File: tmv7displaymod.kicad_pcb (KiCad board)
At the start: 2 copper layers, 70.9 x 33.8 mm, 14 parts, among them J1 DC IN, J2 Conn_01x10, J3 Kenwood CAT Connector, U1 L7805, U4 ATmega8-16P

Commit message: Minor fixes and tweaks
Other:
- board text added: "KENWOOD TM-V7 Display Mod PCB CT1ENQ CT1BDV 2023"
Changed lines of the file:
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@@
   (gr_line (start 147.574 55.372) (end 147.574 89.154)
     (stroke (width 0.1) (type default)) (layer "Edge.Cuts"))
+  (gr_text "KENWOOD TM-V7 Display Mod PCB\n    CT1ENQ CT1BDV 2023" (at 115.57 52.578) (layer "B.Cu")
+    (effects (font (size 1 1) (thickness 0.1875) bold) (justify left bottom mirror))
+  )
   (gr_text "+8 ... 15V" (at 89.154 86.106) (layer "F.SilkS")
     (effects (font (size 1 1) (thickness 0.15)))
@@
   (segment (start 108.839 77.47) (end 109.093 77.216) (width 0.75) (layer "B.Cu") (net 1))
   (segment (start 103.251 77.47) (end 108.839 77.47) (width 1) (layer "B.Cu") (net 1))
-  (segment (start 119.126 83.82) (end 116.84 81.534) (width 1) (layer "B.Cu") (net 2))
-  (segment (start 116.84 81.534) (end 115.951 81.534) (width 1) (layer "B.Cu") (net 2))
-  (segment (start 115.951 81.534) (end 111.633 77.216) (width 1) (layer "B.Cu") (net 2))
+  (segment (start 118.237 83.82) (end 111.633 77.216) (width 1) (layer "B.Cu") (net 2))
+  (segment (start 119.126 83.82) (end 118.237 83.82) (width 1) (layer "B.Cu") (net 2))
   (segment (start 126.746 83.82) (end 126.746 82.296) (width 1) (layer "B.Cu") (net 3))
   (segment (start 126.111 81.661) (end 119.507 81.661) (width 1) (layer "B.Cu") (net 3))

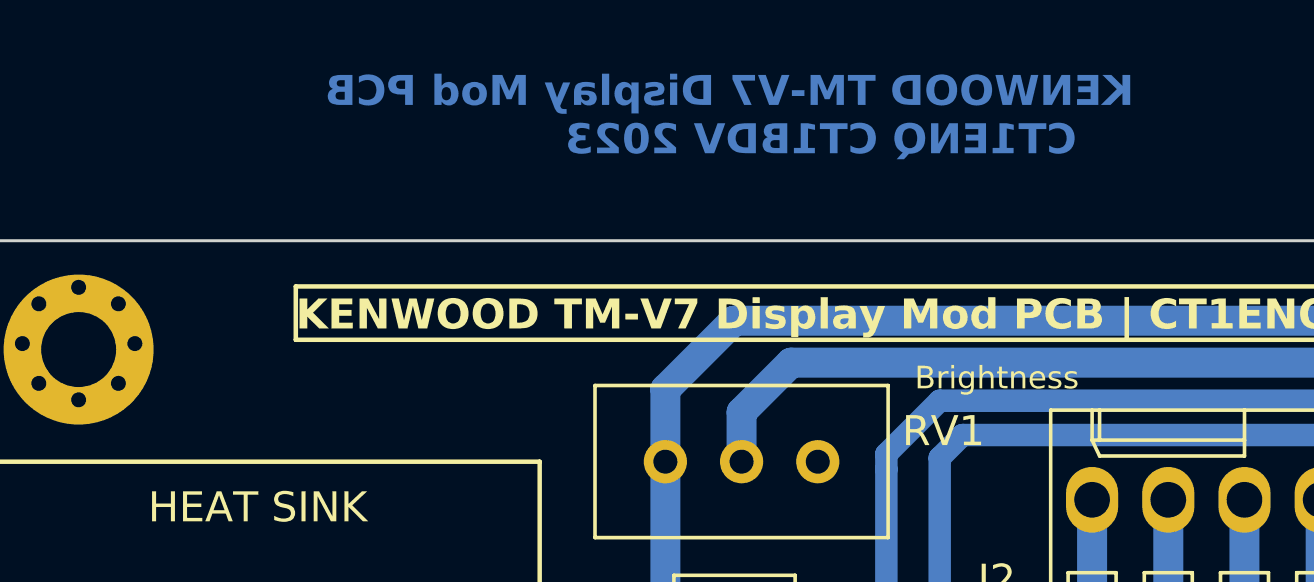
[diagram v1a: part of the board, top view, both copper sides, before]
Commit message: minor tweaks. Brightness was in fact contrast
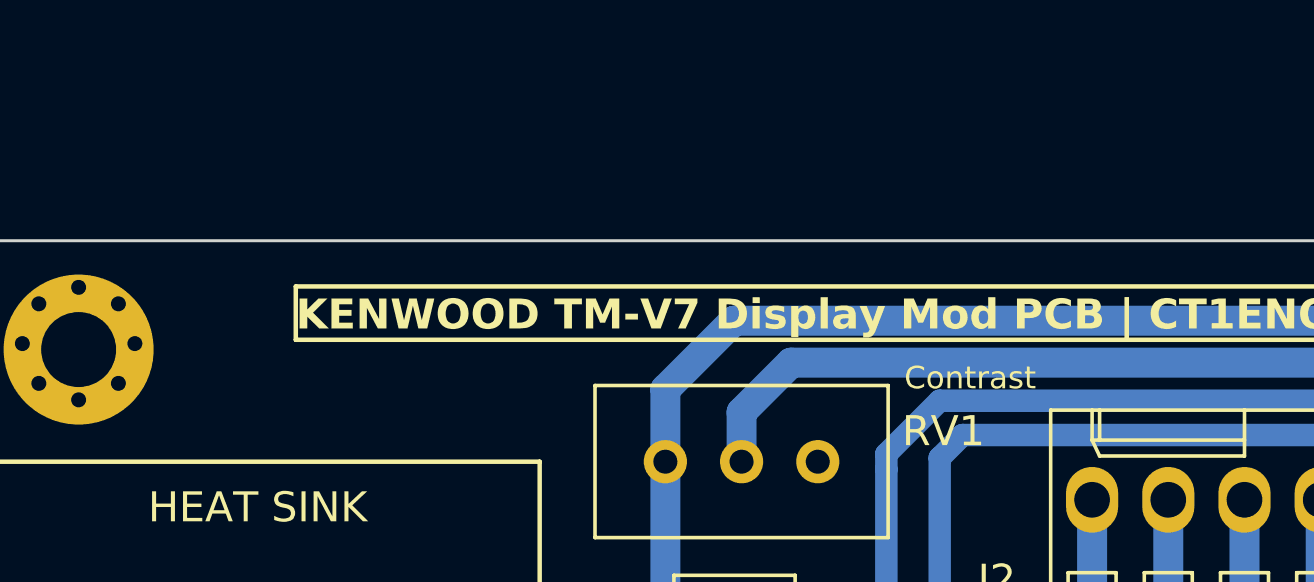
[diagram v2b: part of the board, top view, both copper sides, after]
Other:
- board text added: "Contrast"
- board text removed: "Brightness"
- board text removed: "KENWOOD TM-V7 Display Mod PCB CT1ENQ CT1BDV 2023"
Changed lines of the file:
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@@
   (gr_line (start 147.574 55.372) (end 147.574 89.154)
     (stroke (width 0.1) (type default)) (layer "Edge.Cuts"))
-  (gr_text "KENWOOD TM-V7 Display Mod PCB\n    CT1ENQ CT1BDV 2023" (at 115.57 52.578) (layer "B.Cu")
-    (effects (font (size 1 1) (thickness 0.1875) bold) (justify left bottom mirror))
-  )
   (gr_text "+8 ... 15V" (at 89.154 86.106) (layer "F.SilkS")
     (effects (font (size 1 1) (thickness 0.15)))
@@
     (effects (font (size 1 1) (thickness 0.15)) (justify left bottom))
   )
-  (gr_text "Brightness" (at 110.998 59.944) (layer "F.SilkS")
+  (gr_text "Contrast" (at 110.109 59.944) (layer "F.SilkS")
     (effects (font (size 0.75 0.75) (thickness 0.15)))
   )

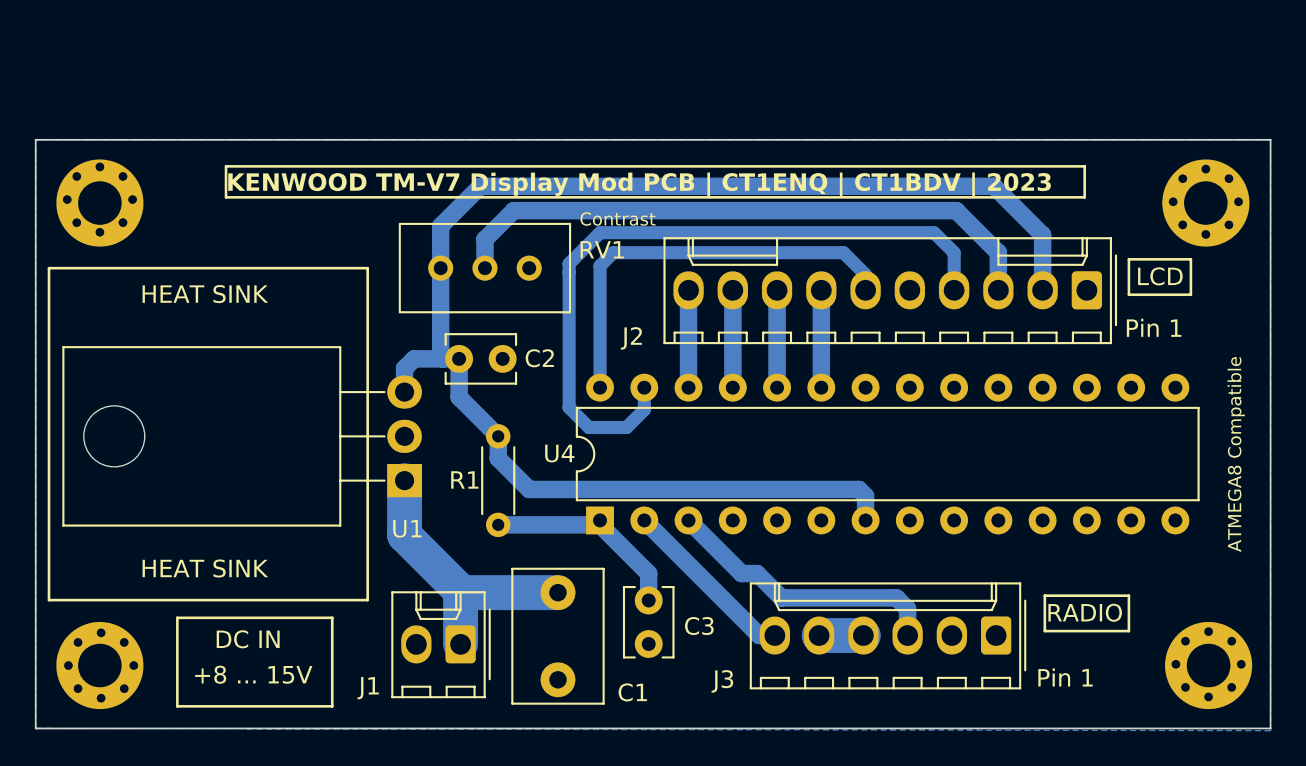
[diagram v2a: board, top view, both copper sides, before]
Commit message: Additional tweaks. xchanged rs for e and added backlight.
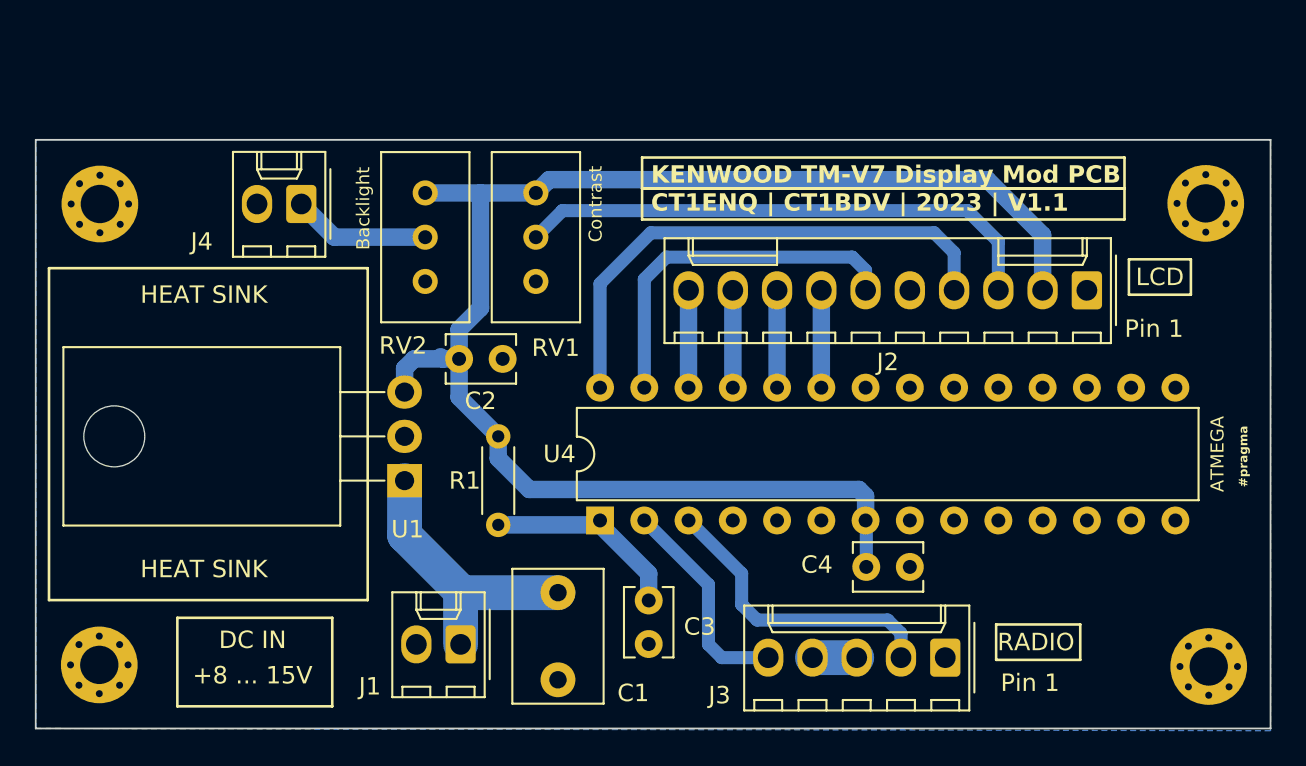
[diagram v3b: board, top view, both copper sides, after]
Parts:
- removed REF** (x4): MountingHole_2.5mm_Pad_Via, MountingHole:MountingHole_2.5mm_Pad_Via
- added C4: 100n, Capacitor_THT:C_Disc_D3.8mm_W2.6mm_P2.50mm, F.Cu at (124.4, 79.9)
- added H1: MountingHole, MountingHole:MountingHole_2.2mm_M2_Pad_Via, F.Cu at (80.4, 59.1)
- added H2: MountingHole, MountingHole:MountingHole_2.2mm_M2_Pad_Via, F.Cu at (143.9, 59.0)
- added H3: MountingHole, MountingHole:MountingHole_2.2mm_M2_Pad_Via, F.Cu at (80.4, 85.5)
- added H4: MountingHole, MountingHole:MountingHole_2.2mm_M2_Pad_Via, F.Cu at (144.0, 85.6)
- added J4: Backlight, Connector_Molex:Molex_KK-254_AE-6410-02A_1x02_P2.54mm_Vertical, F.Cu at (91.9, 59.1)
- added RV2: 10k, Potentiometer_THT:Potentiometer_Bourns_3296W_Vertical, F.Cu at (99.1, 58.4)
- J3: footprint Connector_Molex:Molex_KK-254_AE-6410-06A_1x06_P2.54mm_Vertical -> Connector_Molex:Molex_KK-254_AE-6410-05A_1x05_P2.54mm_Vertical
- RV1: value R_Potentiometer -> 10k
- moved RV1 6.96 mm to (105.4, 58.4), turned to 90 degrees
- moved J3 3.19 mm to (128.9, 85.1)
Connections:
- net LCD_C renamed LCD_CONTRAST
- J2 pad 4: Net-(J2-Pin_4) -> R/S
- J2 pad 6: Net-(J2-Pin_6) -> E
- J3 pad 1: unconnected-(J3-Pin_1-Pad1) -> GND
- J3 pad 2: GND -> MCU_TXD_TO_RIG_PKS_3
- J3 pad 4: Net-(J3-Pin_4) -> Net-(J3-Pin_3)
- J3 pad 5: Net-(J3-Pin_4) -> MCU_RXD_TO_RIG_SQC_6
- U4 pad 2: Net-(J3-Pin_6) -> MCU_RXD_TO_RIG_SQC_6
- U4 pad 27: Net-(J2-Pin_4) -> E
- U4 pad 28: Net-(J2-Pin_6) -> R/S
- U4 pad 3: Net-(J3-Pin_3) -> MCU_TXD_TO_RIG_PKS_3
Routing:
- net Net-(J2-Pin_4): track 40.2 -> 0.00 mm
- net R/S: track 0.00 -> 30.1 mm
- net Net-(J2-Pin_6): track 24.0 -> 0.00 mm
- net E: track 0.00 -> 20.9 mm
- net MCU_TXD_TO_RIG_PKS_3: track 0.00 -> 17.3 mm
- net Net-(J3-Pin_3): track 16.2 -> 2.54 mm
- net MCU_RXD_TO_RIG_SQC_6: track 0.00 -> 12.4 mm
- net Net-(J3-Pin_6): track 10.2 -> 0.00 mm
- net Net-(J4-Pin_1): track 0.00 -> 7.90 mm
- net VCC: track 82.2 -> 87.9 mm
- net LCD_CONTRAST: track 35.0 -> 30.7 mm
- net Net-(J3-Pin_4): track 2.54 -> 0.00 mm
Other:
- board text added: "#pragma"
- board text added: "ATMEGA"
- board text added: "Backlight"
- board text added: "KENWOOD TM-V7 Display Mod PCB CT1ENQ | CT1BDV | 2023 | V1.1"
- board text removed: "ATMEGA8 Compatible"
- board text removed: "KENWOOD TM-V7 Display Mod PCB | CT1ENQ | CT1BDV | 2023"

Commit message: V1.2 - minor tweaks and new exports. Organized exports
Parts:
- added SW1: RESET, Connector_PinHeader_2.54mm:PinHeader_1x02_P2.54mm_Vertical, F.Cu at (116.1, 85.6)
- moved J3 2.92 mm to (131.8, 85.0)
- moved C3 1.16 mm to (111.9, 83.0)
- moved C4 0.13 mm to (124.4, 80.0)
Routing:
- net Net-(U4-PC6/~{RESET}): track 11.4 -> 16.7 mm
- net GND: track 0.00 -> 2.67 mm
- net MCU_RXD_TO_RIG_SQC_6: track 12.4 -> 15.0 mm
- net MCU_TXD_TO_RIG_PKS_3: track 17.3 -> 19.6 mm
- net VCC: track 87.9 -> 87.0 mm
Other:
- board text added: "#pragma 2023"
- board text added: "[- +] [K A]"
- board text removed: "#pragma"
- board text removed: "KENWOOD TM-V7 Display Mod PCB CT1ENQ | CT1BDV | 2023 | V1.1"

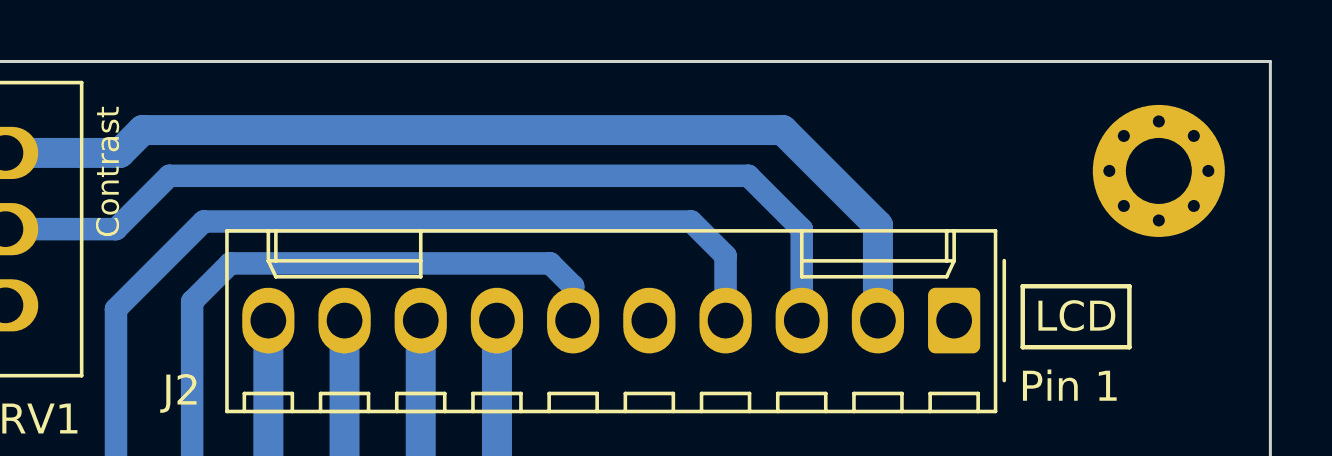
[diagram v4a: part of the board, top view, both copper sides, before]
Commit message: Fixed missing callsigns in silkcreen layer
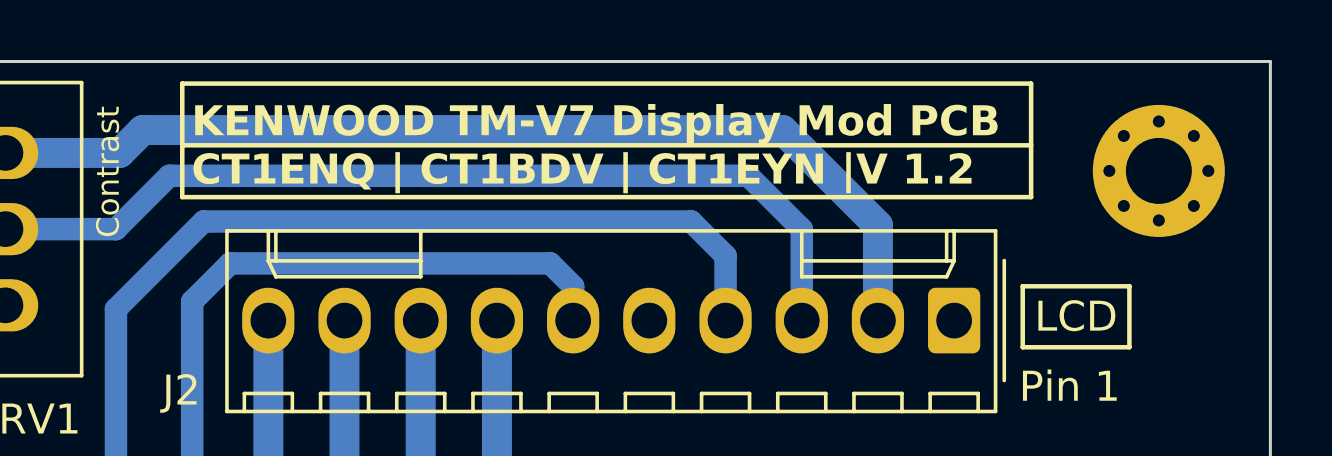
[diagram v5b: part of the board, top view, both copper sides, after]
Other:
- board text added: "KENWOOD TM-V7 Display Mod PCB CT1ENQ | CT1BDV | CT1EYN |V 1.2"
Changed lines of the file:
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@@
   (gr_rect (start 77.47 62.738) (end 95.758 81.788)
     (stroke (width 0.15) (type default)) (fill none) (layer "F.SilkS"))
+  (gr_rect (start 111.3028 56.1086) (end 139.5984 59.8932)
+    (stroke (width 0.15) (type default)) (fill none) (layer "F.SilkS"))
+  (gr_line (start 139.5984 58.166) (end 111.3028 58.166)
+    (stroke (width 0.15) (type default)) (layer "F.SilkS"))
   (gr_rect (start 139.319 62.865) (end 142.875 64.897)
     (stroke (width 0.15) (type default)) (fill none) (layer "F.SilkS"))
@@
     (effects (font (size 1 1) (thickness 0.15)) (justify left bottom))
   )
+  (gr_text "KENWOOD TM-V7 Display Mod PCB\nCT1ENQ | CT1BDV | CT1EYN |V 1.2" (at 111.6076 59.563) (layer "F.SilkS")
+    (effects (font (size 1 1) (thickness 0.25) bold) (justify left bottom))
+  )
   (gr_text "Contrast" (at 108.839 59.055 90) (layer "F.SilkS")

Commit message: Exported output for v1.3
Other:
- board text added: "CT1ENQ CT1EYN CT1BDV"
- board text added: "KENWOOD TM-V7 Display Mod PCB CT1ENQ | CT1BDV | CT1EYN |V 1.3"
- board text removed: "KENWOOD TM-V7 Display Mod PCB CT1ENQ | CT1BDV | CT1EYN |V 1.2"
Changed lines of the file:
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@@
   (gr_line (start 147.574 55.372) (end 147.574 89.154)
     (stroke (width 0.1) (type default)) (layer "Edge.Cuts"))
+  (gr_text "CT1ENQ\nCT1EYN\nCT1BDV" (at 94.742 87.884) (layer "B.Cu")
+    (effects (font (size 1.5 1.5) (thickness 0.3) bold) (justify left bottom mirror))
+  )
   (gr_text "+8 ... 15V" (at 89.154 86.106) (layer "F.SilkS")
     (effects (font (size 1 1) (thickness 0.15)))
@@
     (effects (font (size 1 1) (thickness 0.15)) (justify left bottom))
   )
-  (gr_text "KENWOOD TM-V7 Display Mod PCB\nCT1ENQ | CT1BDV | CT1EYN |V 1.2" (at 111.6076 59.563) (layer "F.SilkS")
+  (gr_text "KENWOOD TM-V7 Display Mod PCB\nCT1ENQ | CT1BDV | CT1EYN |V 1.3" (at 111.6076 59.563) (layer "F.SilkS")
     (effects (font (size 1 1) (thickness 0.25) bold) (justify left bottom))
   )
